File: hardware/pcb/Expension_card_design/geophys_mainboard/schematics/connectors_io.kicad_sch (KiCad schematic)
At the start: 15 parts, among them J2 USB_C_Receptacle_USB2.0_16P, Q1 AO3400A

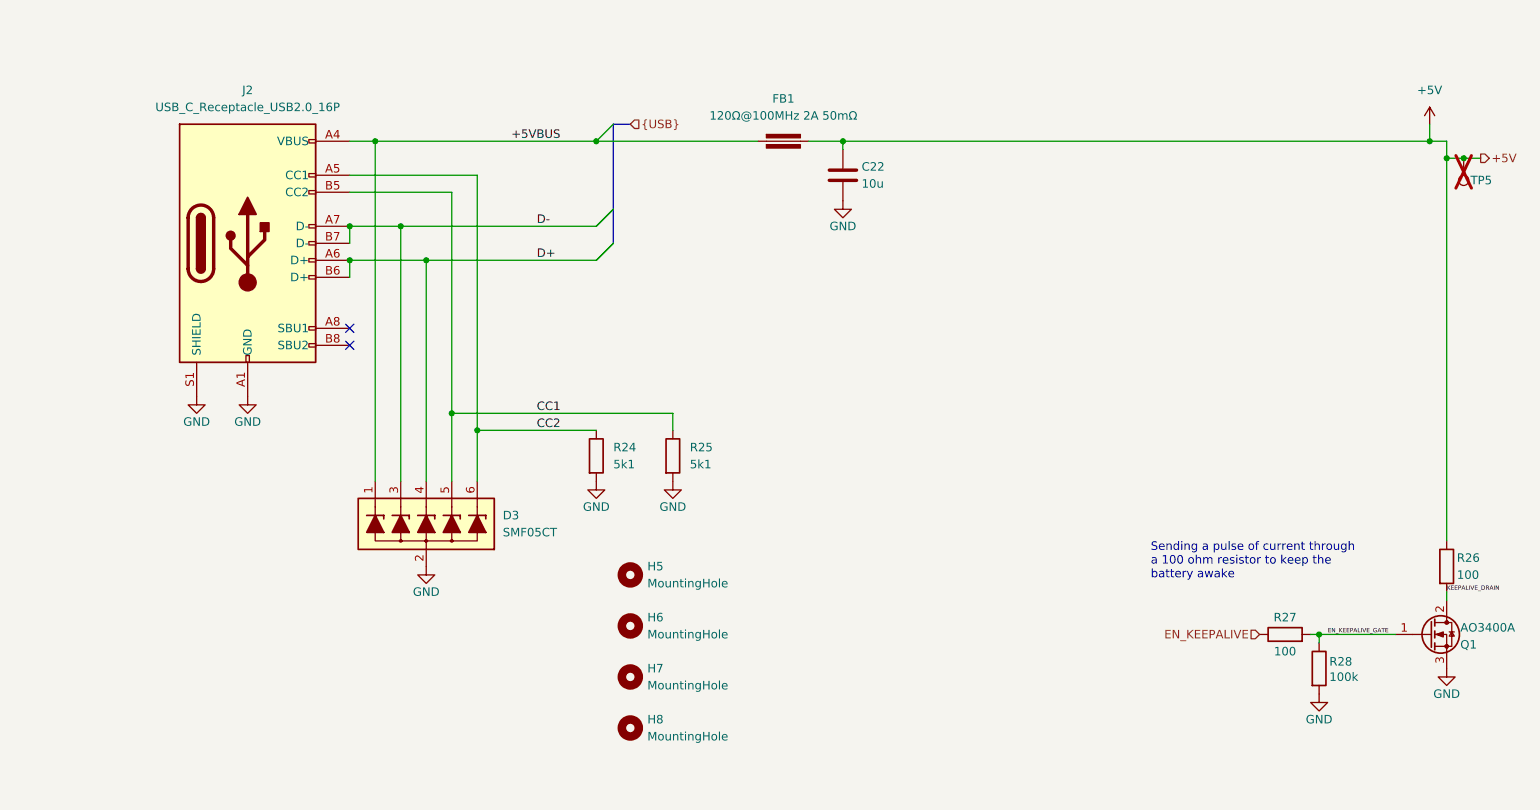
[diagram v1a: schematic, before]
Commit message: Backup avant deletion offset/dac
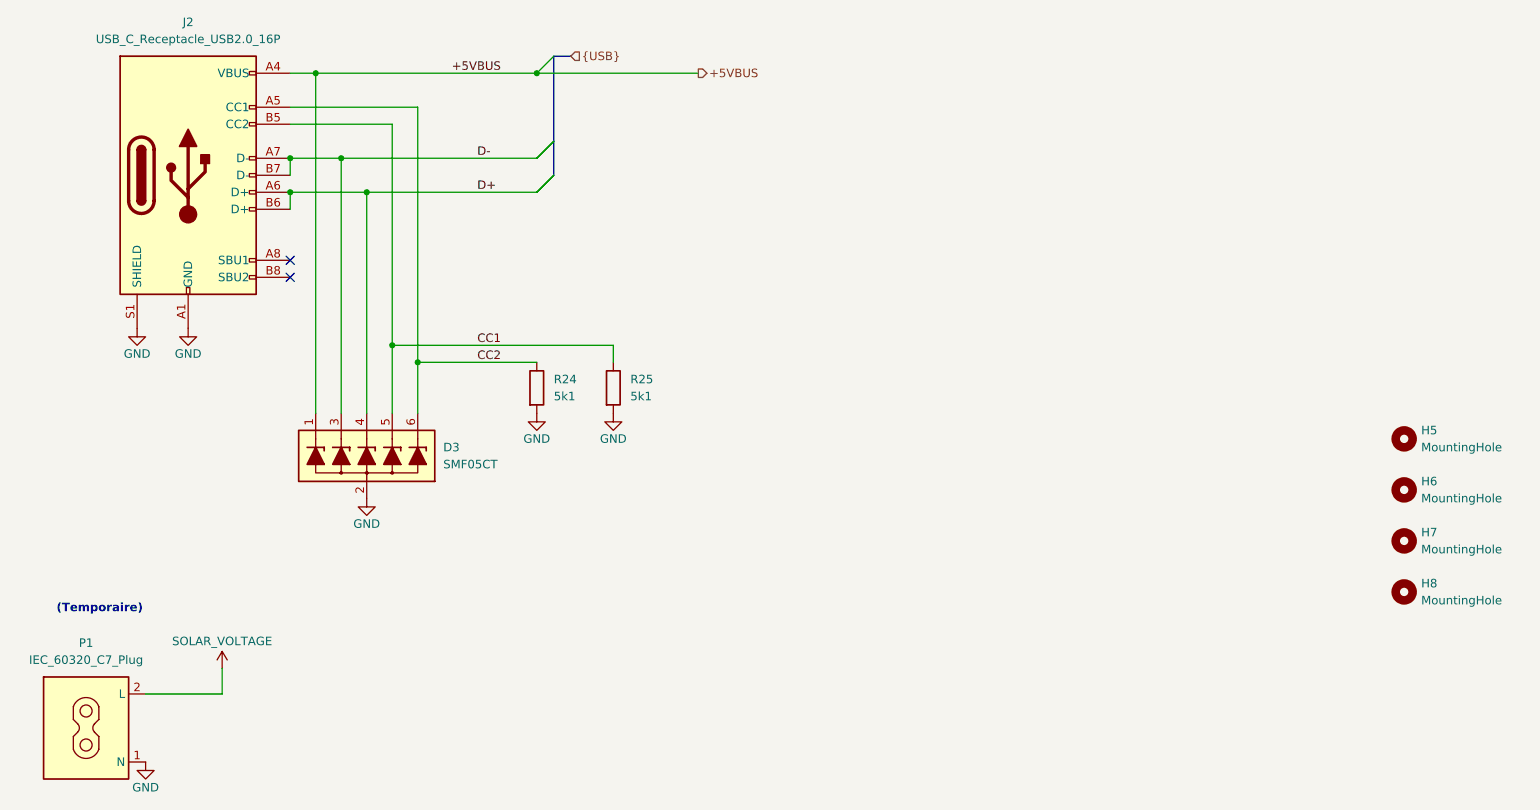
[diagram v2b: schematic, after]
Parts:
- removed C22: 10u, Capacitor_SMD:C_0805_2012Metric, symbol Device:C
- removed FB1: 120Ω@100MHz 2A 50mΩ, Inductor_SMD:L_0603_1608Metric, symbol PCM_Device_AKL:Ferrite_Bead
- removed Q1: AO3400A, Package_TO_SOT_SMD:SOT-23, symbol magnode_symbols:AO3400A
- removed R26, R27: 100, Resistor_SMD:R_0603_1608Metric, symbol Device:R
- removed R28: 100k, Resistor_SMD:R_0603_1608Metric, symbol Device:R
- removed TP5: TestPoint, TestPoint:TestPoint_THTPad_1.0x1.0mm_Drill0.5mm, symbol Connector:TestPoint
- added P1: IEC_60320_C7_Plug, symbol Connector:IEC_60320_C7_Plug
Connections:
- net GND: now also P1.1 (N)
- new net SOLAR_VOLTAGE: P1.2 (L)
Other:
- note added: "(Temporaire)"
- note removed: "Sending a pulse of current through a 100 ohm resistor to keep the battery awake"
- moved on the sheet: D3, H5, H6, H7, H8, J2, R24, R25
